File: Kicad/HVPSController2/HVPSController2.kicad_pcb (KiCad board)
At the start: 4 copper layers, 314.1 x 184 mm, 178 parts, among them J1 Vsupply, J10 Tap debug pin, J11 USB RWGBS, J12 USB RWGBS, J13 Conn_01x01_Pin, J14 Conn_01x01_Pin, J15 Tap, J16 Tap debug pin, J17 Conn_01x02_Pin, J2 GND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

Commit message: Put in place emulation of the ESP32 FPGA interface in C#.
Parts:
- removed J24: Standoff Hole, Custom:ContactViaM3
- R23: footprint Resistor_THT:R_Axial_DIN0207_L6.3mm_D2.5mm_P5.08mm_Vertical -> Resistor_THT:R_Axial_DIN0207_L6.3mm_D2.5mm_P7.62mm_Horizontal; moved to B.Cu
- moved U25 9.69 mm to (218.5, 92.9)
- moved G*** 7.44 mm to (177.9, 198.6)
- moved R23 6.82 mm to (243.7, 123.9), turned to -135 degrees
- moved U2 4.56 mm to (94.9, 163.8)
- moved R29 4.50 mm to (216.8, 97.0)
- moved R24 2.47 mm to (243.7, 193.8), turned to 180 degrees
- moved R35 1.52 mm to (210.2, 201.1)
- moved L2 0.85 mm to (203.7, 79.1)
- moved C13 0.20 mm to (72.7, 165.2)
- moved C19 0.20 mm to (72.7, 157.7)
- moved C25 0.20 mm to (72.7, 172.9)
- moved OR3 0.20 mm to (64.2, 162.2)
- moved OT3 0.20 mm to (64.2, 174.4)
- turned R31 to 130 degrees
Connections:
- net +14V renamed /15V_2
- C20 pad 1: +3V3 -> /3v3_2
- C21 pad 1: +3V3 -> /3v3_2
- C22 pad 1: +3V3 -> /3v3_2
- C26 pad 1: +3V3 -> /3v3_2
- C27 pad 1: +3V3 -> /3v3_2
- C55 pad 1: +3V3 -> /3v3_2
- C56 pad 1: +3V3 -> /3v3_2
- C69 pad 1: +3V3 -> /3v3_2
- C70 pad 1: +3V3 -> /3v3_2
- C74 pad 1: Net-(U24-COM) -> Earth
- J4 pad 1: +3V3 -> /3v3_2
- J8 pad 2: +3V3 -> /3v3_2
- OR4 pad 3: +3V3 -> /3v3_2
- OR5 pad 3: +3V3 -> /3v3_2
- OR6 pad 3: +3V3 -> /3v3_2
- OT4 pad 2: +3V3 -> /3v3_2
- OT5 pad 2: +3V3 -> /3v3_2
- R10 pad 1: +3V3 -> /3v3_2
- R14 pad 1: +3V3 -> /3v3_2
- R9 pad 1: +3V3 -> /3v3_2
- U12 pad 14: +3V3 -> /3v3_2
- U23 pad 9: +3V3 -> /3v3_2
- U24 pad 2: Net-(U24-COM) -> Earth
- U3 pad 4: +3V3 -> /3v3_2
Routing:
- net +3V3: track 824.0 -> 468.1 mm
- net /3v3_2: track 0.00 -> 351.6 mm
- net +36V: track 541.0 -> 421.0 mm
- net Net-(H3-Pin_1): track 133.9 -> 38.2 mm
- net Net-(J14-Pin_1): track 46.8 -> 0.00 mm
- net Net-(H4-Pin_1): track 82.6 -> 37.9 mm
- net Net-(U2-VP_a1i): track 13.4 -> 7.51 mm
- net Net-(OR3-Vout): track 34.2 -> 28.9 mm
- net Net-(OT1-Vin): track 74.0 -> 68.8 mm
- net Net-(OT3-Vin): track 36.1 -> 31.2 mm
- net Net-(OT2-Vin): track 61.4 -> 56.5 mm
- net Net-(U2-3V3): track 29.2 -> 24.6 mm
- net Net-(U2-D32_a1io): track 50.1 -> 54.3 mm
- net Net-(OR2-Vout): track 71.1 -> 67.0 mm
- net Net-(J4-Pin_4): track 44.8 -> 48.7 mm
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- added copper zone on B.Cu, net +36V
- added copper zone on In2.Cu, net Earth
- added copper zone on B.Cu, net Net-(H3-Pin_1)
- added copper zone on F.Cu, net Net-(H3-Pin_1)
- added copper zone on B.Cu, net Net-(H4-Pin_1)
- added copper zone on F.Cu, net Net-(H4-Pin_1)
- added copper zone on B.Cu, net Net-(J14-Pin_1)
- added copper zone on F.Cu, net Net-(J14-Pin_1)
- removed copper zone on B.Cu, net Earth
- removed copper zone on F.Cu, net Earth
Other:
- board text added: "14V"
- board text added: "15V"
- board text added: "Channel 1"
- board text added: "Channel 2"
- board text added: "Channel 3"

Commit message: Board almost done got some more checks to do first been cleaning up nicely.
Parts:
- added J24: Conn_01x02_Pin, Connector_JST:JST_XH_B2B-XH-A_1x02_P2.50mm_Vertical, F.Cu at (209.4, 120.6)
- added J3: Snubber, Custom:Snubber_Connection_1, B.Cu at (244.2, 135.8)
- added J5: Snubber, Custom:Snubber_Connection_1, B.Cu at (244.0, 204.8)
- added J6: Snubber, Custom:Snubber_Connection_1, B.Cu at (210.1, 130.1)
- added J7: Snubber, Custom:Snubber_Connection_1, B.Cu at (219.5, 199.2)
- R34: moved to B.Cu
- S2: footprint Custom:SLW-1678105-6A-N-D -> Custom:MSS-04A
- moved J17 5.49 mm to (200.0, 120.6)
- moved R3 4.29 mm to (95.9, 189.4)
- moved R6 4.29 mm to (98.6, 181.7)
- moved C38 4.29 mm to (98.0, 175.6)
- moved D4 4.29 mm to (96.0, 178.7)
- moved R4 4.29 mm to (105.6, 171.9)
- moved S2 3.75 mm to (67.5, 145.8)
- moved J19 2.74 mm to (212.7, 185.8)
- moved J18 2.66 mm to (213.5, 145.9)
- moved J11 2.45 mm to (60.0, 130.9)
- moved J12 2.45 mm to (71.0, 130.9)
- moved D3 1.76 mm to (291.9, 114.6)
- moved D15 1.24 mm to (237.5, 211.7)
- moved R37 1.24 mm to (222.4, 211.7)
- moved D14 1.21 mm to (237.0, 115.9)
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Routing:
- net Net-(J17-Pin_1): track 11.1 -> 21.8 mm
- net +36V: track 421.0 -> 412.1 mm
- net /3v3_2: track 351.6 -> 344.4 mm
- net Net-(U2-VP_a1i): track 7.51 -> 12.1 mm
- net +3V3: track 468.1 -> 472.5 mm
- net Net-(D3-K): track 224.4 -> 227.6 mm
- net Net-(D3-A): track 11.5 -> 14.5 mm
- net Net-(J12-Pin_1): track 12.4 -> 10.1 mm
- net Net-(U2-3V3): track 24.6 -> 22.9 mm
- net Net-(D14-K): track 7.53 -> 8.75 mm
- net Net-(H3-Pin_1): track 38.2 -> 37.0 mm
- net Net-(OR2-Vout): track 67.0 -> 68.0 mm
- net Net-(D15-K): track 7.58 -> 8.61 mm
- net +15V: track 30.0 -> 29.3 mm
- net Net-(H4-Pin_1): track 37.9 -> 38.5 mm

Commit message: Going great think im ready to order the pcb!
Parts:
- added J27: ~, Connector_PinHeader_2.54mm:PinHeader_1x01_P2.54mm_Vertical, F.Cu at (193.8, 156.2)
- added J28: ~, Connector_PinHeader_2.54mm:PinHeader_1x01_P2.54mm_Vertical, F.Cu at (193.8, 167.0)
- added J29: ~, Connector_PinHeader_2.54mm:PinHeader_1x01_P2.54mm_Vertical, F.Cu at (352.2, 94.2)
- added J30: ~, Connector_PinHeader_2.54mm:PinHeader_1x01_P2.54mm_Vertical, F.Cu at (352.2, 98.8)
- added J31: ~, Connector_PinHeader_2.54mm:PinHeader_1x01_P2.54mm_Vertical, F.Cu at (352.2, 103.5)
- added J32: Conn_01x02_Pin, Connector_PinHeader_2.54mm:PinHeader_1x02_P2.54mm_Vertical, F.Cu at (92.8, 196.2)
- added J33: Conn_01x02_Pin, Connector_PinHeader_2.54mm:PinHeader_1x02_P2.54mm_Vertical, F.Cu at (185.5, 124.0)
- added J34: Conn_01x02_Pin, Connector_PinHeader_2.54mm:PinHeader_1x02_P2.54mm_Vertical, F.Cu at (114.5, 101.0)
- added J35: Conn_01x02_Pin, Connector_PinHeader_2.54mm:PinHeader_1x02_P2.54mm_Vertical, F.Cu at (223.0, 105.0)
- added J36: Conn_01x02_Pin, Connector_PinHeader_2.54mm:PinHeader_1x02_P2.54mm_Vertical, F.Cu at (208.8, 209.8)
- J10, J16: value Tap debug pin -> Conn_01x02_Pin; footprint Connector_PinHeader_2.54mm:PinHeader_1x01_P2.54mm_Vertical -> Connector_PinHeader_2.54mm:PinHeader_1x02_P2.54mm_Vertical
- R34: footprint Resistor_THT:R_Axial_DIN0207_L6.3mm_D2.5mm_P7.62mm_Horizontal -> Resistor_THT:R_Axial_DIN0207_L6.3mm_D2.5mm_P5.08mm_Vertical; moved to F.Cu
- moved J8 8.53 mm to (87.6, 107.0), turned to -90 degrees
- moved R5 6.01 mm to (300.2, 95.0)
- moved R7 6.01 mm to (298.0, 100.2)
- moved R24 5.11 mm to (239.7, 197.0), turned to 40 degrees
- moved R8 4.46 mm to (307.8, 91.8), turned to 180 degrees
- moved R10 3.94 mm to (85.8, 102.8)
- moved U1 3.31 mm to (309.0, 98.0), turned to -90 degrees
- moved R9 3.14 mm to (90.4, 112.0)
- moved J24 1.66 mm to (211.0, 120.6)
- moved R34 1.32 mm to (215.2, 128.8), turned to 160 degrees
- moved U31 1.00 mm to (195.0, 224.0)
- moved D6 0.55 mm to (125.9, 233.1)
- moved J17 0.54 mm to (200.5, 120.6)
- moved L2 0.50 mm to (203.7, 79.6)
- moved G*** 0.32 mm to (178.2, 198.5)
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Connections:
- J8 pad 3: Net-(J4-Pin_3) -> Net-(J4-Pin_4)
- J8 pad 4: Net-(J4-Pin_4) -> Net-(J4-Pin_3)
- R24 pad 1: Net-(U22-G) -> Net-(H4-Pin_1)
- R24 pad 2: Net-(H4-Pin_1) -> Net-(U22-G)
- U12 pad 9: Earth -> /3v3_2
- U20 pad 9: Earth -> +3V3
- U5 pad 9: Earth -> +3V3
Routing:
- net +3V3: track 472.5 -> 503.8 mm
- net +5V: track 185.1 -> 199.6 mm
- net /15V_2: track 18.8 -> 27.0 mm
- net Net-(U2-D21_io): track 252.3 -> 258.2 mm
- net Net-(D7-K): track 36.7 -> 40.7 mm
- net Net-(H4-Pin_1): track 38.5 -> 35.5 mm
- net Net-(D3-A): track 14.5 -> 11.5 mm
- net Net-(J4-Pin_3): track 52.4 -> 50.1 mm
- net +15V: track 29.3 -> 31.5 mm
- net Net-(J17-Pin_1): track 21.8 -> 23.6 mm
- net Net-(J4-Pin_4): track 48.7 -> 47.5 mm
- net /3v3_2: track 344.4 -> 343.5 mm
- net Earth: track 34.1 -> 33.3 mm, vias 3 -> 4
- net Net-(U1-G): track 8.42 -> 9.24 mm
- net Net-(D6-A): track 57.7 -> 57.1 mm
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- added copper zone on F.Cu, net (none)
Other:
- board text added: "I2C: SCL, SDA, +, GND"
- board text added: "MPU-6500"
- board text added: "Receivers (FPGA)"
- board text added: "Transmitters (FPGA)"
- board text added: "USB"

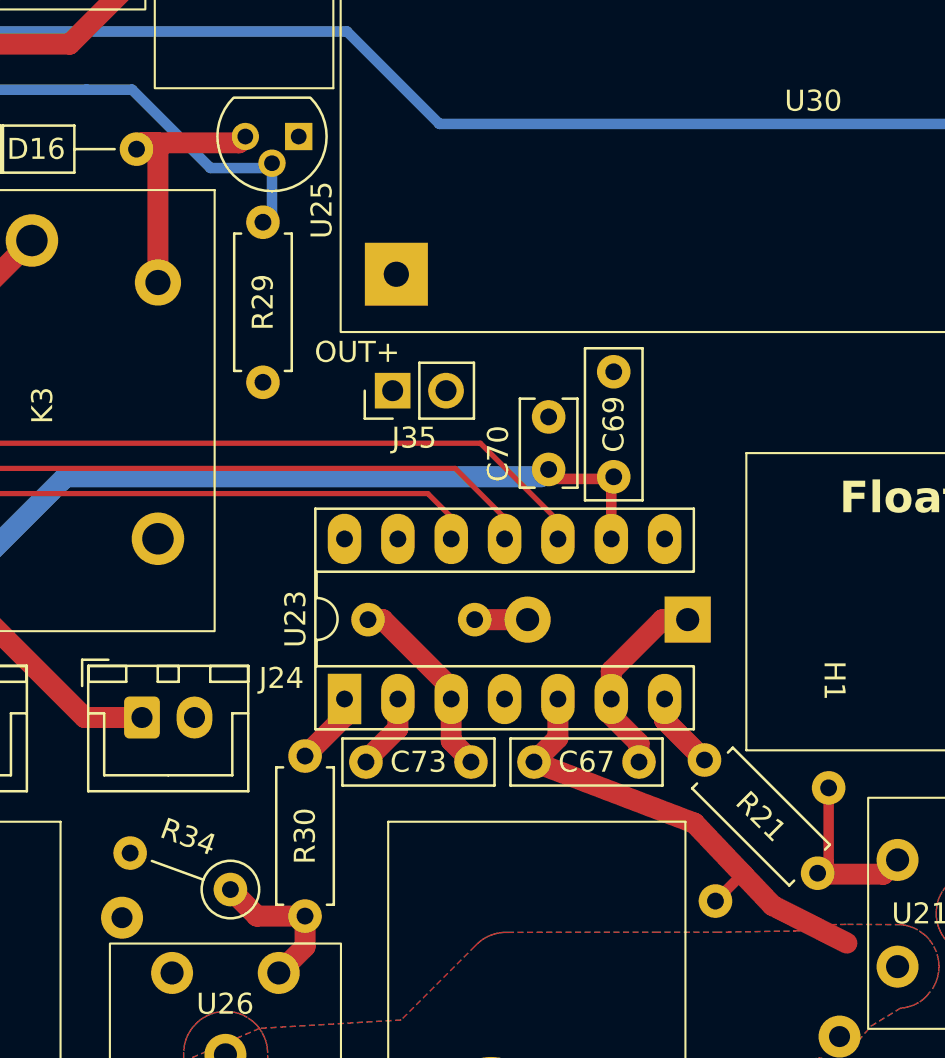
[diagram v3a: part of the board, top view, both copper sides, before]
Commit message: Working on the automatic generation of the fpga interface for microcontroller to speak to fpga. C++ microcontroller side almost done :)
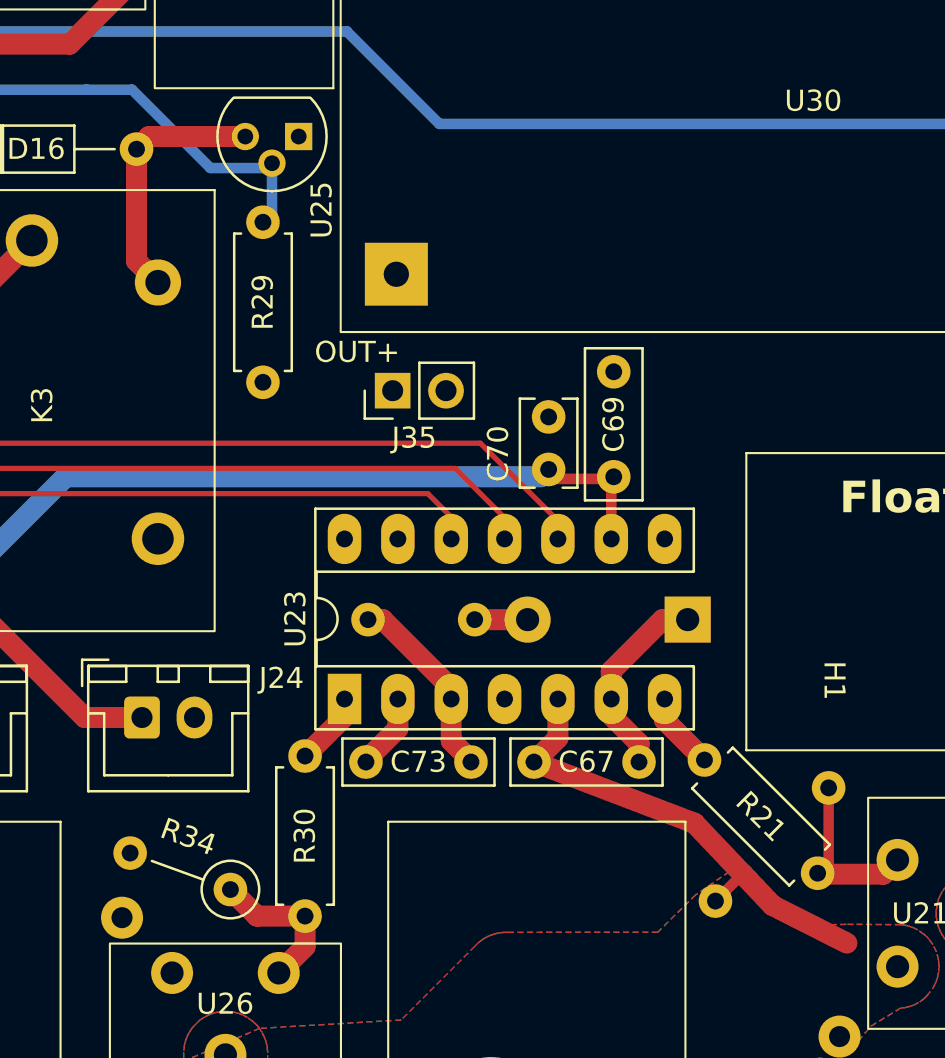
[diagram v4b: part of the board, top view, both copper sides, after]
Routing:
- net Net-(D16-A): track 12.8 -> 12.2 mm
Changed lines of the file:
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@@
 		)
 		(fp_text user "${REFERENCE}"
-			(at 0 1.27 360)
+			(at 0 1.27 0)
 			(layer "F.Fab")
 			(effects
@@
 		(tags "Resistor Axial_DIN0207 series Axial Horizontal pin pitch 7.62mm 0.25W = 1/4W length 6.3mm diameter 2.5mm")
 		(property "Reference" "R8"
-			(at 3.81 -0.1 360)
+			(at 3.81 -0.1 0)
 			(layer "F.SilkS")
 			(effects
@@
 		)
 		(property "Value" "10K"
-			(at 3.81 2.37 360)
+			(at 3.81 2.37 0)
 			(layer "F.Fab")
 			(effects
@@
 		)
 		(fp_text user "${REFERENCE}"
-			(at 3.81 0 360)
+			(at 3.81 0 0)
 			(layer "F.Fab")
 			(effects
@@
 		)
 		(property "Value" "1000"
-			(at 2.54 2.37 160)
+			(at 2.540001 2.37 160)
 			(layer "F.Fab")
 			(effects
@@
 		)
 		(fp_text user "${REFERENCE}"
-			(at 0 1.27 360)
+			(at 0 1.27 0)
 			(layer "F.Fab")
 			(effects
@@
 	)
 	(segment
-		(start 221.3 115.9)
-		(end 218.4 113)
+		(start 221.15 115.9)
+		(end 222 115.9)
 		(width 1)
 		(layer "In2.Cu")
@@
 	)
 	(segment
-		(start 222.5 104.525)
-		(end 222.5 103)
-		(width 0.5)
+		(start 221.95 103.55)
+		(end 218.4 107.1)
+		(width 1)
 		(layer "In2.Cu")
 		(net 93)
 	)
 	(segment
-		(start 218.4 113)
-		(end 218.4 107.1)
+		(start 218.4 113.15)
+		(end 221.15 115.9)
 		(width 1)
 		(layer "In2.Cu")
@@
 	)
 	(segment
-		(start 222 115.9)
-		(end 221.3 115.9)
-		(width 1)
+		(start 221.95 103.55)
+		(end 221.95 103.975)
+		(width 0.5)
 		(layer "In2.Cu")
 		(net 93)
@@
 	(segment
 		(start 218.4 107.1)
-		(end 222.5 103)
+		(end 218.4 113.15)
 		(width 1)
 		(layer "In2.Cu")
@@
 	)
 	(segment
-		(start 222.975 105)
-		(end 222.5 104.525)
-		(width 0.5)
+		(start 223 102.5)
+		(end 223 99.7075)
+		(width 1)
 		(layer "In2.Cu")
 		(net 93)
 	)
 	(segment
-		(start 222.5 103)
-		(end 223 102.5)
-		(width 1)
+		(start 221.95 103.975)
+		(end 222.975 105)
+		(width 0.5)
 		(layer "In2.Cu")
 		(net 93)
 	)
 	(segment
-		(start 223 102.5)
-		(end 223 99.7075)
+		(start 221.95 103.55)
+		(end 223 102.5)
 		(width 1)
 		(layer "In2.Cu")
@@
 	)
 	(segment
-		(start 211.08 93.2)
-		(end 215.66 93.2)
+		(start 210.78 93.5)
+		(end 211.08 93.2)
 		(width 1)
 		(layer "F.Cu")
@@
 	)
 	(segment
-		(start 210.78 93.5)
-		(end 211.08 93.2)
+		(start 211.8 99.85)
+		(end 210.78 98.83)
 		(width 1)
 		(layer "F.Cu")
@@
 	)
 	(segment
-		(start 215.66 93.2)
-		(end 215.96 92.9)
+		(start 211.08 93.2)
+		(end 211.38 92.9)
 		(width 1)
 		(layer "F.Cu")
@@
 	)
 	(segment
-		(start 211.8 99.85)
-		(end 211.8 93.2)
+		(start 211.38 92.9)
+		(end 215.96 92.9)
 		(width 1)
 		(layer "F.Cu")
@@
 	)
 	(segment
-		(start 211.8 93.2)
-		(end 211.08 93.2)
+		(start 210.78 98.83)
+		(end 210.78 93.5)
 		(width 1)
 		(layer "F.Cu")
@@
 				(xy 248.87 131.72) (xy 248.69 131.37) (xy 248.51 131.12) (xy 248.4 131) (xy 248.28 130.89) (xy 247.97 130.67)
 				(xy 247.77 130.57) (xy 247.57 130.5) (xy 247.38 130.45) (xy 247.17 130.42) (xy 244.91 130.41) (xy 244.57 130.41)
-				(xy 243.27 130.43) (xy 242.32 130.72) (xy 238.49 130.78) (xy 235.6 130.78)
+				(xy 243.27 130.43) (xy 242.2 129.7) (xy 241.3 129.1) (xy 239.9 127.6) (xy 239 127.9) (xy 237.4 129)
+				(xy 235.6 130.78)
 			)
 		)
